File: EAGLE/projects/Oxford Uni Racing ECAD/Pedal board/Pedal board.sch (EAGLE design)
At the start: 40 parts, among them IC1 AD711N, J1 ASS + BOTS, J2 THR_1_2, J3 PWR_CAN, J6 BR_POS_PRESS_STWH, J7 T821108A1S100CEU, K2 EC2-12TNU, T1 BT169, X2 D-SUB9-H2M09ST

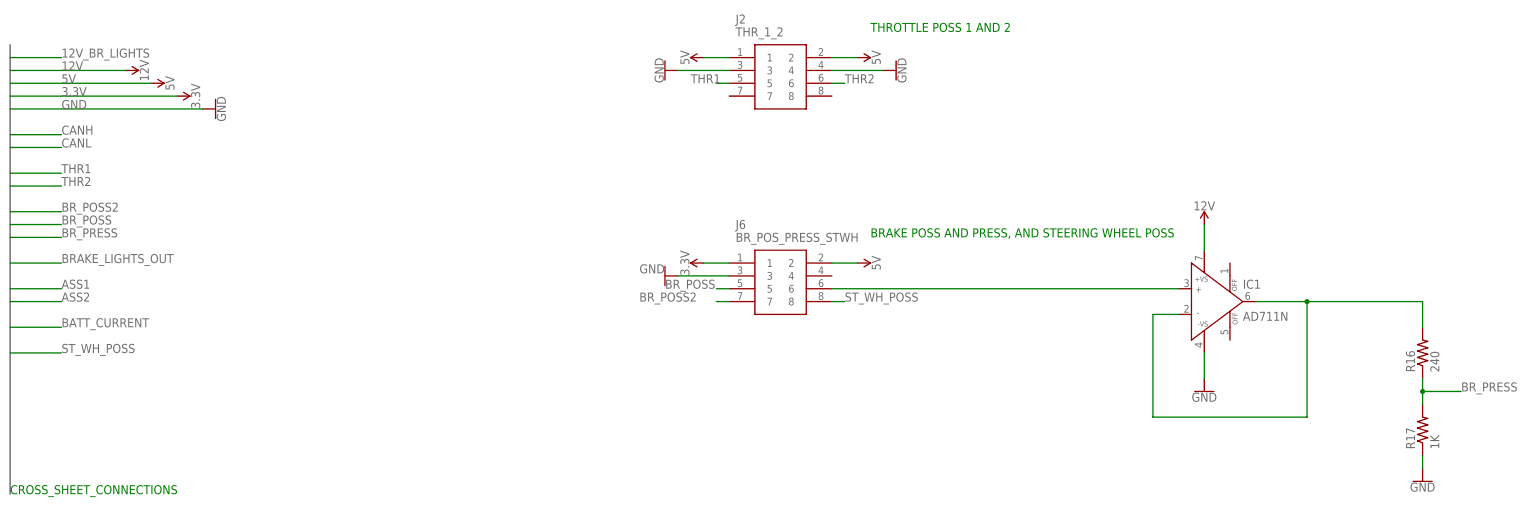
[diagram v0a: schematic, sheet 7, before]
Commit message: added 1M pullup resistors to analog sensors
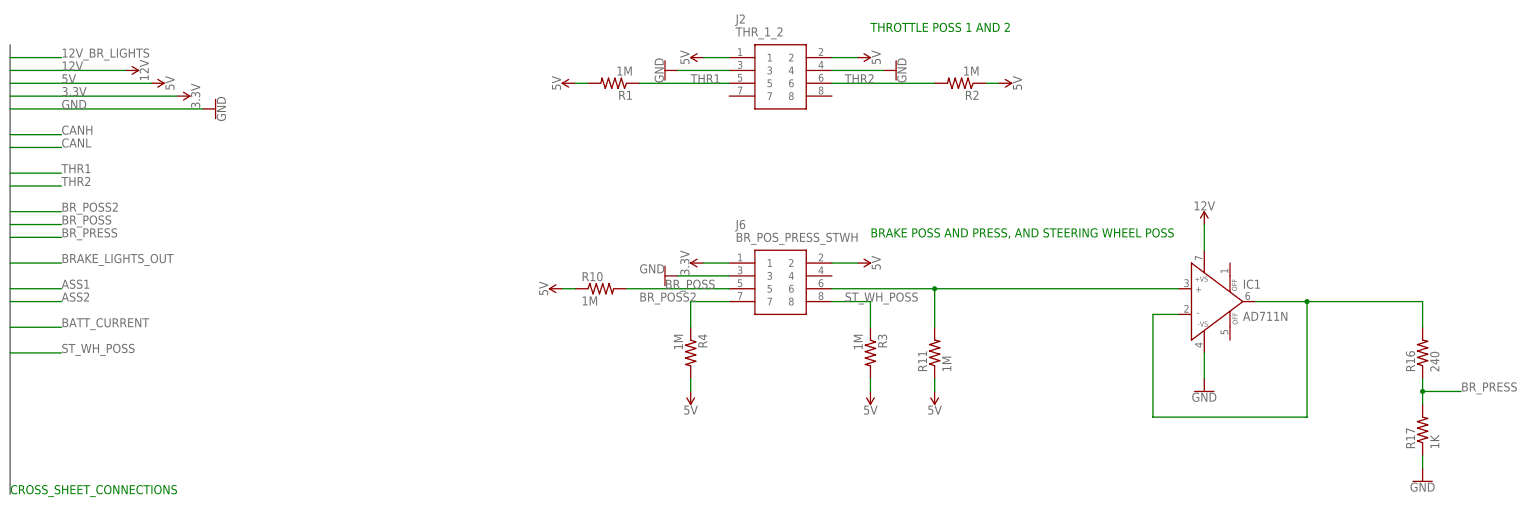
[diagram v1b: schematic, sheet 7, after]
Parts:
- added R1, R10, R11, R2, R3, R4: 1M, adafruit:R-US_0204/7
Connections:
- net 5V: now also R1.2, R10.1, R11.1, R2.1, R3.2, R4.2
- net BR_POSS: now also R10.2
- net BR_POSS2: now also R4.1
- net N$27: now also R11.2
- net ST_WH_POSS: now also R3.1
- net THR1: now also R1.1
- net THR2: now also R2.2
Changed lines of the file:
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@@
 <part name="F1" library="fuse" library_urn="urn:adsk.eagle:library:233" deviceset="FUSE" device="BLANK_5X20MM" package3d_urn="urn:adsk.eagle:package:14079/1" value="1A"/>
 <part name="BRAKE_LIGHTS" library="fuse" library_urn="urn:adsk.eagle:library:233" deviceset="FUSE" device="BLANK_5X20MM" package3d_urn="urn:adsk.eagle:package:14079/1" value="2A"/>
+<part name="R1" library="adafruit" library_urn="urn:adsk.eagle:library:420" deviceset="R-US_" device="0204/7" package3d_urn="urn:adsk.eagle:package:6240596/1" value="1M"/>
+<part name="R2" library="adafruit" library_urn="urn:adsk.eagle:library:420" deviceset="R-US_" device="0204/7" package3d_urn="urn:adsk.eagle:package:6240596/1" value="1M"/>
+<part name="R3" library="adafruit" library_urn="urn:adsk.eagle:library:420" deviceset="R-US_" device="0204/7" package3d_urn="urn:adsk.eagle:package:6240596/1" value="1M"/>
+<part name="R4" library="adafruit" library_urn="urn:adsk.eagle:library:420" deviceset="R-US_" device="0204/7" package3d_urn="urn:adsk.eagle:package:6240596/1" value="1M"/>
+<part name="R10" library="adafruit" library_urn="urn:adsk.eagle:library:420" deviceset="R-US_" device="0204/7" package3d_urn="urn:adsk.eagle:package:6240596/1" value="1M"/>
+<part name="R11" library="adafruit" library_urn="urn:adsk.eagle:library:420" deviceset="R-US_" device="0204/7" package3d_urn="urn:adsk.eagle:package:6240596/1" value="1M"/>
+<part name="SUPPLY11" library="SparkFun-PowerSymbols" library_urn="urn:adsk.eagle:library:530" deviceset="5V" device=""/>
+<part name="SUPPLY19" library="SparkFun-PowerSymbols" library_urn="urn:adsk.eagle:library:530" deviceset="5V" device=""/>
+<part name="SUPPLY42" library="SparkFun-PowerSymbols" library_urn="urn:adsk.eagle:library:530" deviceset="5V" device=""/>
+<part name="SUPPLY43" library="SparkFun-PowerSymbols" library_urn="urn:adsk.eagle:library:530" deviceset="5V" device=""/>
+<part name="SUPPLY44" library="SparkFun-PowerSymbols" library_urn="urn:adsk.eagle:library:530" deviceset="5V" device=""/>
+<part name="SUPPLY45" library="SparkFun-PowerSymbols" library_urn="urn:adsk.eagle:library:530" deviceset="5V" device=""/>
 </parts>
 <sheets>
@@
 <attribute name="VALUE" x="170.434" y="86.36" size="1.778" layer="96" rot="R270" align="bottom-center"/>
 </instance>
+<instance part="R1" gate="G$1" x="119.38" y="81.28" smashed="yes" rot="R180">
+<attribute name="NAME" x="123.19" y="79.7814" size="1.778" layer="95" rot="R180"/>
+<attribute name="VALUE" x="123.19" y="84.582" size="1.778" layer="96" rot="R180"/>
+</instance>
+<instance part="R2" gate="G$1" x="187.96" y="81.28" smashed="yes" rot="R180">
+<attribute name="NAME" x="191.77" y="79.7814" size="1.778" layer="95" rot="R180"/>
+<attribute name="VALUE" x="191.77" y="84.582" size="1.778" layer="96" rot="R180"/>
+</instance>
+<instance part="R3" gate="G$1" x="170.18" y="27.94" smashed="yes" rot="R270">
+<attribute name="NAME" x="171.6786" y="31.75" size="1.778" layer="95" rot="R270"/>
+<attribute name="VALUE" x="166.878" y="31.75" size="1.778" layer="96" rot="R270"/>
+</instance>
+<instance part="R4" gate="G$1" x="134.62" y="27.94" smashed="yes" rot="R270">
+<attribute name="NAME" x="136.1186" y="31.75" size="1.778" layer="95" rot="R270"/>
+<attribute name="VALUE" x="131.318" y="31.75" size="1.778" layer="96" rot="R270"/>
+</instance>
+<instance part="R10" gate="G$1" x="116.84" y="40.64" smashed="yes">
+<attribute name="NAME" x="113.03" y="42.1386" size="1.778" layer="95"/>
+<attribute name="VALUE" x="113.03" y="37.338" size="1.778" layer="96"/>
+</instance>
+<instance part="R11" gate="G$1" x="182.88" y="27.94" smashed="yes" rot="R90">
+<attribute name="NAME" x="181.3814" y="24.13" size="1.778" layer="95" rot="R90"/>
+<attribute name="VALUE" x="186.182" y="24.13" size="1.778" layer="96" rot="R90"/>
+</instance>
+<instance part="SUPPLY11" gate="G$1" x="111.76" y="81.28" smashed="yes" rot="R90">
+<attribute name="VALUE" x="108.966" y="81.28" size="1.778" layer="96" rot="R90" align="bottom-center"/>
+</instance>
+<instance part="SUPPLY19" gate="G$1" x="109.22" y="40.64" smashed="yes" rot="R90">
+<attribute name="VALUE" x="106.426" y="40.64" size="1.778" layer="96" rot="R90" align="bottom-center"/>
+</instance>
+<instance part="SUPPLY42" gate="G$1" x="195.58" y="81.28" smashed="yes" rot="R270">
+<attribute name="VALUE" x="198.374" y="81.28" size="1.778" layer="96" rot="R270" align="bottom-center"/>
+</instance>
+<instance part="SUPPLY43" gate="G$1" x="182.88" y="20.32" smashed="yes" rot="R180">
+<attribute name="VALUE" x="182.88" y="17.526" size="1.778" layer="96" rot="R180" align="bottom-center"/>
+</instance>
+<instance part="SUPPLY44" gate="G$1" x="170.18" y="20.32" smashed="yes" rot="R180">
+<attribute name="VALUE" x="170.18" y="17.526" size="1.778" layer="96" rot="R180" align="bottom-center"/>
+</instance>
+<instance part="SUPPLY45" gate="G$1" x="134.62" y="20.32" smashed="yes" rot="R180">
+<attribute name="VALUE" x="134.62" y="17.526" size="1.778" layer="96" rot="R180" align="bottom-center"/>
+</instance>
 </instances>
 <busses>
@@
 <pinref part="SUPPLY9" gate="G$1" pin="5V"/>
 </segment>
+<segment>
+<pinref part="R10" gate="G$1" pin="1"/>
+<pinref part="SUPPLY19" gate="G$1" pin="5V"/>
+<wire x1="111.76" y1="40.64" x2="109.22" y2="40.64" width="0.1524" layer="91"/>
+</segment>
+<segment>
+<pinref part="R4" gate="G$1" pin="2"/>
+<pinref part="SUPPLY45" gate="G$1" pin="5V"/>
+<wire x1="134.62" y1="22.86" x2="134.62" y2="20.32" width="0.1524" layer="91"/>
+</segment>
+<segment>
+<pinref part="R11" gate="G$1" pin="1"/>
+<pinref part="SUPPLY43" gate="G$1" pin="5V"/>
+<wire x1="182.88" y1="22.86" x2="182.88" y2="20.32" width="0.1524" layer="91"/>
+</segment>
+<segment>
+<pinref part="R3" gate="G$1" pin="2"/>
+<pinref part="SUPPLY44" gate="G$1" pin="5V"/>
+<wire x1="170.18" y1="22.86" x2="170.18" y2="20.32" width="0.1524" layer="91"/>
+</segment>
+<segment>
+<pinref part="R2" gate="G$1" pin="1"/>
+<pinref part="SUPPLY42" gate="G$1" pin="5V"/>
+<wire x1="193.04" y1="81.28" x2="195.58" y2="81.28" width="0.1524" layer="91"/>
+</segment>
+<segment>
+<pinref part="R1" gate="G$1" pin="2"/>
+<pinref part="SUPPLY11" gate="G$1" pin="5V"/>
+<wire x1="114.3" y1="81.28" x2="111.76" y2="81.28" width="0.1524" layer="91"/>
+</segment>
 </net>
 <net name="3.3V" class="0">
@@
 <segment>
 <pinref part="J2" gate="G$1" pin="5"/>
-<wire x1="142.24" y1="81.28" x2="139.7" y2="81.28" width="0.1524" layer="91"/>
 <label x="134.62" y="81.28" size="1.778" layer="95"/>
+<pinref part="R1" gate="G$1" pin="1"/>
+<wire x1="142.24" y1="81.28" x2="124.46" y2="81.28" width="0.1524" layer="91"/>
 </segment>
 </net>
@@
 <segment>
 <pinref part="J2" gate="G$1" pin="6"/>
-<wire x1="162.56" y1="81.28" x2="165.1" y2="81.28" width="0.1524" layer="91"/>
 <label x="165.1" y="81.28" size="1.778" layer="95"/>
+<pinref part="R2" gate="G$1" pin="2"/>
+<wire x1="162.56" y1="81.28" x2="182.88" y2="81.28" width="0.1524" layer="91"/>
 </segment>
 </net>
@@
 <segment>
 <pinref part="J6" gate="G$1" pin="5"/>
-<wire x1="142.24" y1="40.64" x2="139.7" y2="40.64" width="0.1524" layer="91"/>
 <label x="129.54" y="40.64" size="1.778" layer="95"/>
+<pinref part="R10" gate="G$1" pin="2"/>
+<wire x1="142.24" y1="40.64" x2="121.92" y2="40.64" width="0.1524" layer="91"/>
 </segment>
 </net>
@@
 <segment>
 <pinref part="J6" gate="G$1" pin="8"/>
-<wire x1="162.56" y1="38.1" x2="165.1" y2="38.1" width="0.1524" layer="91"/>
 <label x="165.1" y="38.1" size="1.778" layer="95"/>
+<pinref part="R3" gate="G$1" pin="1"/>
+<wire x1="170.18" y1="33.02" x2="170.18" y2="38.1" width="0.1524" layer="91"/>
+<wire x1="170.18" y1="38.1" x2="162.56" y2="38.1" width="0.1524" layer="91"/>
 </segment>
 </net>
@@
 <pinref part="J6" gate="G$1" pin="6"/>
 <pinref part="IC1" gate="G$1" pin="IN+"/>
-<wire x1="162.56" y1="40.64" x2="231.14" y2="40.64" width="0.1524" layer="91"/>
+<wire x1="162.56" y1="40.64" x2="182.88" y2="40.64" width="0.1524" layer="91"/>
+<pinref part="R11" gate="G$1" pin="2"/>
+<wire x1="182.88" y1="40.64" x2="231.14" y2="40.64" width="0.1524" layer="91"/>
+<wire x1="182.88" y1="33.02" x2="182.88" y2="40.64" width="0.1524" layer="91"/>
+<junction x="182.88" y="40.64"/>
 </segment>
 </net>
@@
 <segment>
 <pinref part="J6" gate="G$1" pin="7"/>
-<wire x1="142.24" y1="38.1" x2="139.7" y2="38.1" width="0.1524" layer="91"/>
 <label x="124.46" y="38.1" size="1.778" layer="95"/>
-</segment>
-<segment>
+<pinref part="R4" gate="G$1" pin="1"/>
+<wire x1="134.62" y1="33.02" x2="134.62" y2="38.1" width="0.1524" layer="91"/>
+<wire x1="134.62" y1="38.1" x2="142.24" y2="38.1" width="0.1524" layer="91"/>
+</segment>
+<segment>

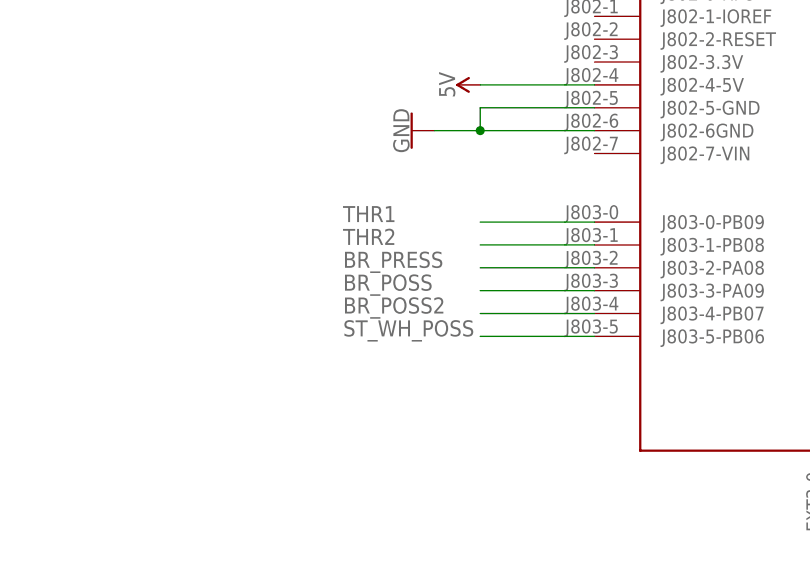
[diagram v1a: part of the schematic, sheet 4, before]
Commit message: fixed overlapping digital pins
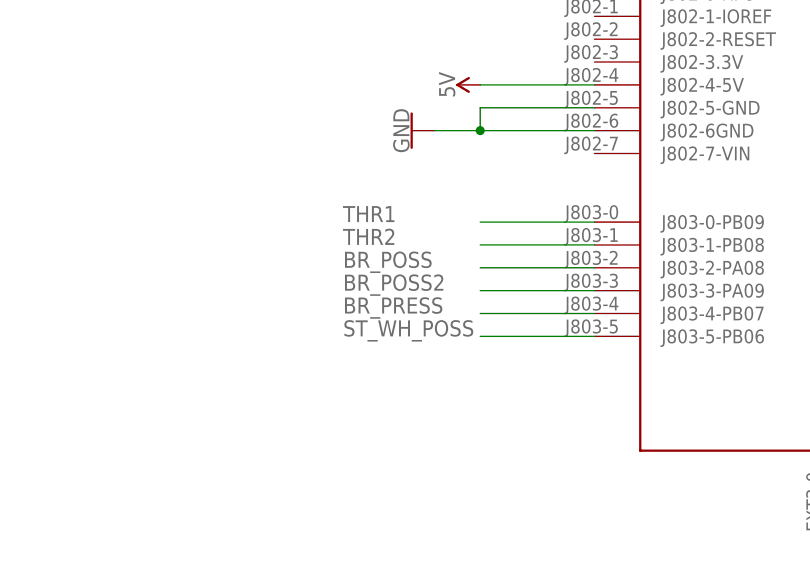
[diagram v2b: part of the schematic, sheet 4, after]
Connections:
- net BR_POSS: now also U$1.J803-2-PA08; no longer U$1.J803-3-PA09
- net BR_POSS2: now also U$1.J803-3-PA09; no longer U$1.J803-4-PB07
- net BR_PRESS: now also U$1.J803-4-PB07; no longer U$1.J803-2-PA08
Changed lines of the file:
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@@
 </segment>
 <segment>
-<pinref part="U$1" gate="G$1" pin="J803-3-PA09"/>
-<wire x1="175.26" y1="10.16" x2="162.56" y2="10.16" width="0.1524" layer="91"/>
-<label x="147.32" y="10.16" size="1.778" layer="95"/>
+<pinref part="U$1" gate="G$1" pin="J803-2-PA08"/>
+<wire x1="175.26" y1="12.7" x2="162.56" y2="12.7" width="0.1524" layer="91"/>
+<label x="147.32" y="12.7" size="1.778" layer="95"/>
 </segment>
 </net>
@@
 </segment>
 <segment>
-<pinref part="U$1" gate="G$1" pin="J803-2-PA08"/>
-<wire x1="175.26" y1="12.7" x2="162.56" y2="12.7" width="0.1524" layer="91"/>
-<label x="147.32" y="12.7" size="1.778" layer="95"/>
+<pinref part="U$1" gate="G$1" pin="J803-4-PB07"/>
+<wire x1="175.26" y1="7.62" x2="162.56" y2="7.62" width="0.1524" layer="91"/>
+<label x="147.32" y="7.62" size="1.778" layer="95"/>
 </segment>
 </net>
@@
 </segment>
 <segment>
-<pinref part="U$1" gate="G$1" pin="J803-4-PB07"/>
-<wire x1="175.26" y1="7.62" x2="162.56" y2="7.62" width="0.1524" layer="91"/>
-<label x="147.32" y="7.62" size="1.778" layer="95"/>
+<pinref part="U$1" gate="G$1" pin="J803-3-PA09"/>
+<wire x1="175.26" y1="10.16" x2="162.56" y2="10.16" width="0.1524" layer="91"/>
+<label x="147.32" y="10.16" size="1.778" layer="95"/>
 </segment>
 </net>
